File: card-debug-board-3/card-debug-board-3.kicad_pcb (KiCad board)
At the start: 4 copper layers, 54 x 64 mm, 101 parts, among them J1 USB4105-GF-A, J2 USB4105-GF-A, J3 Conn_01x05, J4 5040501291, J5 2-1734592-0, Q1 PMV450ENEAR, Q2 PMV450ENEAR, Q3 NTR4101P, SW1 B3F-1000, SW2 PCM13SMTR, SW3 B3F-1000, SW4 SW_DIP_x01, U1 MIC5205-3.3YM5, U2 W25Q16JVSS, U3 RP2040, U4 74AUP1G17, U5 74AUP1G17, U6 IP4234CZ6,125, U7 IP4234CZ6,125, Y1 12 MHz

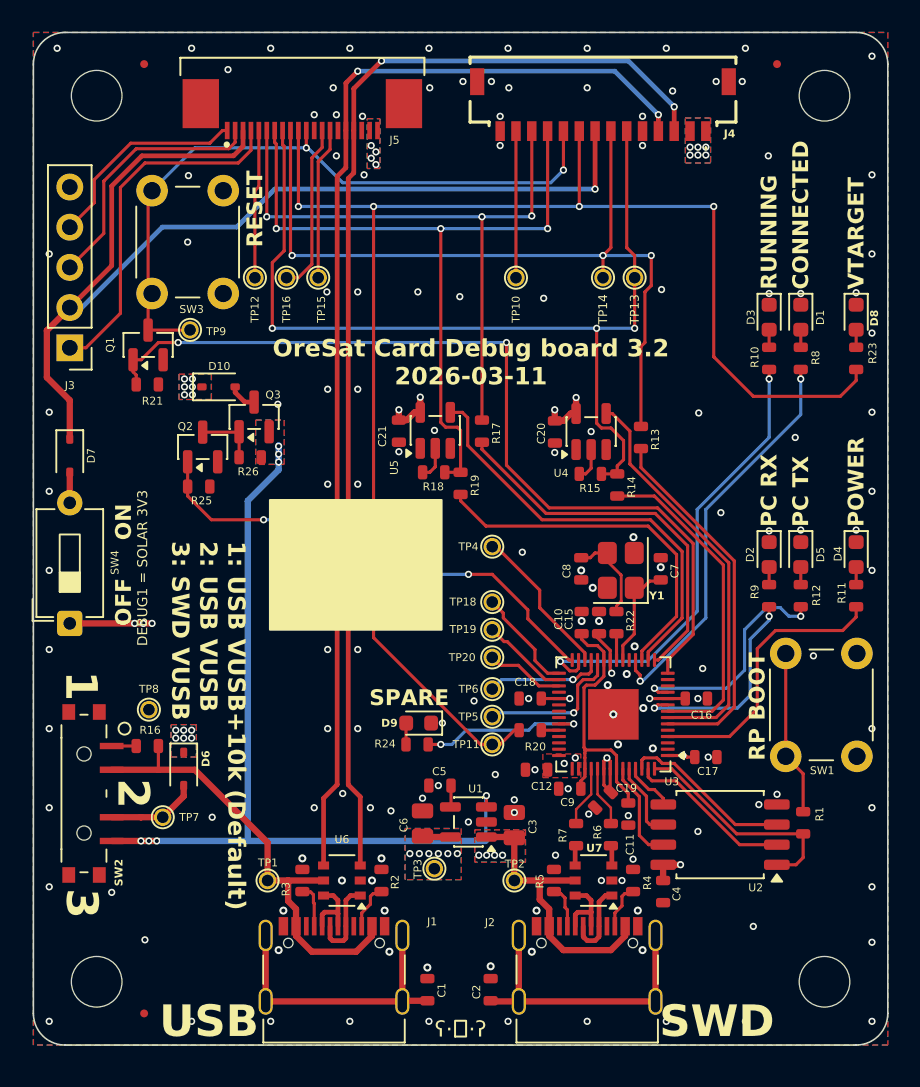
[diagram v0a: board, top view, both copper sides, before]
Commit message: v3.3 of the card debug board, now with automativ solar power control
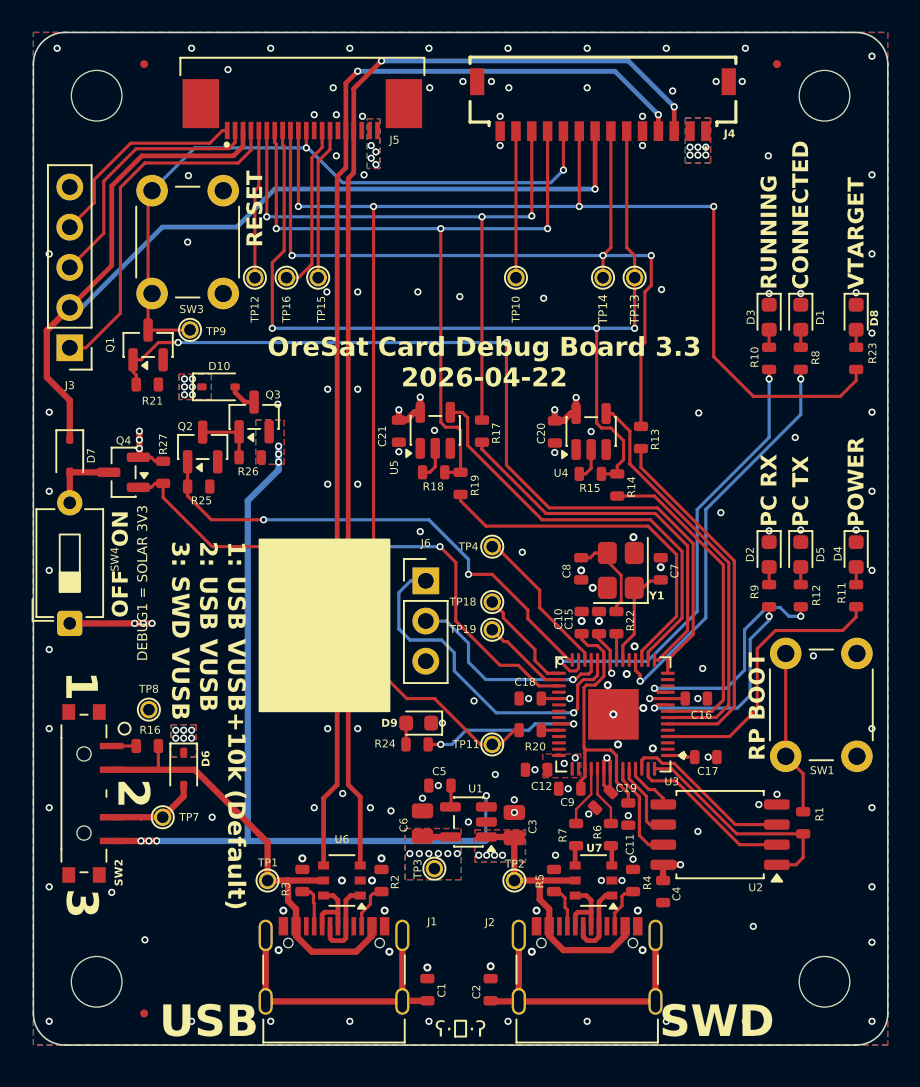
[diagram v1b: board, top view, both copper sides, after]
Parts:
- removed TP20, TP5, TP6: TestPoint-MinTH, oresat-misc:TestPoint-MinTH
- added J6: Conn_01x03, Connector_PinHeader_2.54mm:PinHeader_1x03_P2.54mm_Vertical, F.Cu at (170.8, 80.7)
- added Q4: DMP2035UQ-7, Package_TO_SOT_SMD:SOT-23, F.Cu at (151.7, 73.8)
- added R27: 10k, oresat-passives:0603-C-NOSILK, F.Cu at (154.2, 73.8)
- Q1, Q2: value PMV450ENEAR -> DMN3028LQ-7
- Q3: value NTR4101P -> DMP2035UQ-7
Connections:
- U3 pad 31: Net-(U3-GPIO20) -> /TARGET_POWER_SOLAR
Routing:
- net /TARGET_POWER_SOLAR: track 0.00 -> 34.7 mm, vias 0 -> 2
- net Net-(J6-Pin_1): track 9.59 -> 22.6 mm
- net Net-(J6-Pin_2): track 7.45 -> 13.6 mm
- net Net-(U3-GPIO20): track 4.96 -> 0.00 mm
- net +3.3V: track 28.9 -> 32.3 mm, vias 21 -> 24
- net Net-(D7-A): track 1.93 -> 4.39 mm
- net /VTARGET: track 96.1 -> 97.1 mm
- net /TARGET_POWER: track 31.1 -> 31.7 mm
- net GND: vias 152 -> 151
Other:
- board text added: "OreSat Card Debug Board ${REVISION} ${ISSUE_DATE}"
- board text removed: "OreSat Card Debug board ${REVISION} ${ISSUE_DATE}"
- board text removed: "SPARE"

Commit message: Commits for v3.3 fabrication
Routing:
- net Net-(J2-SHIELD): track 18.8 -> 27.5 mm
